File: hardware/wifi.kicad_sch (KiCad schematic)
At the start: 29 parts, among them J1 RJ45_Hanrun_HR913550A_Horizon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, U3 AP6212, Y1 26MHz

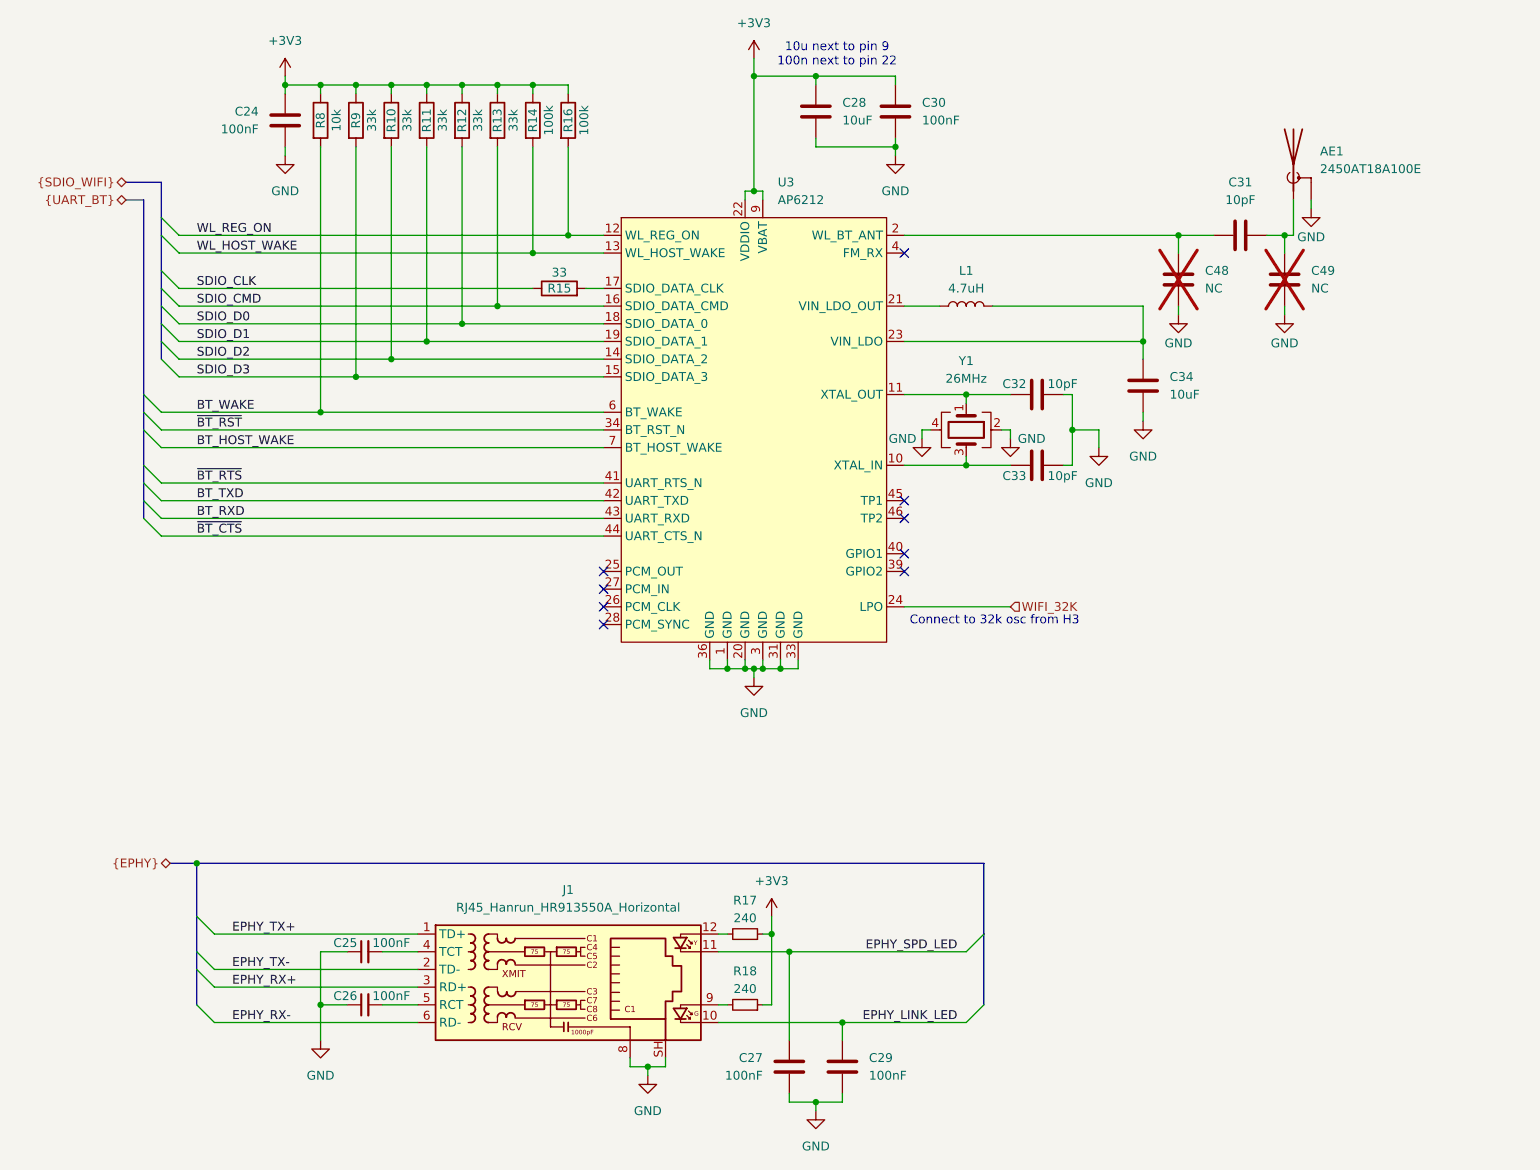
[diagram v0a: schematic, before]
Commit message: Drew most of DC DC converters
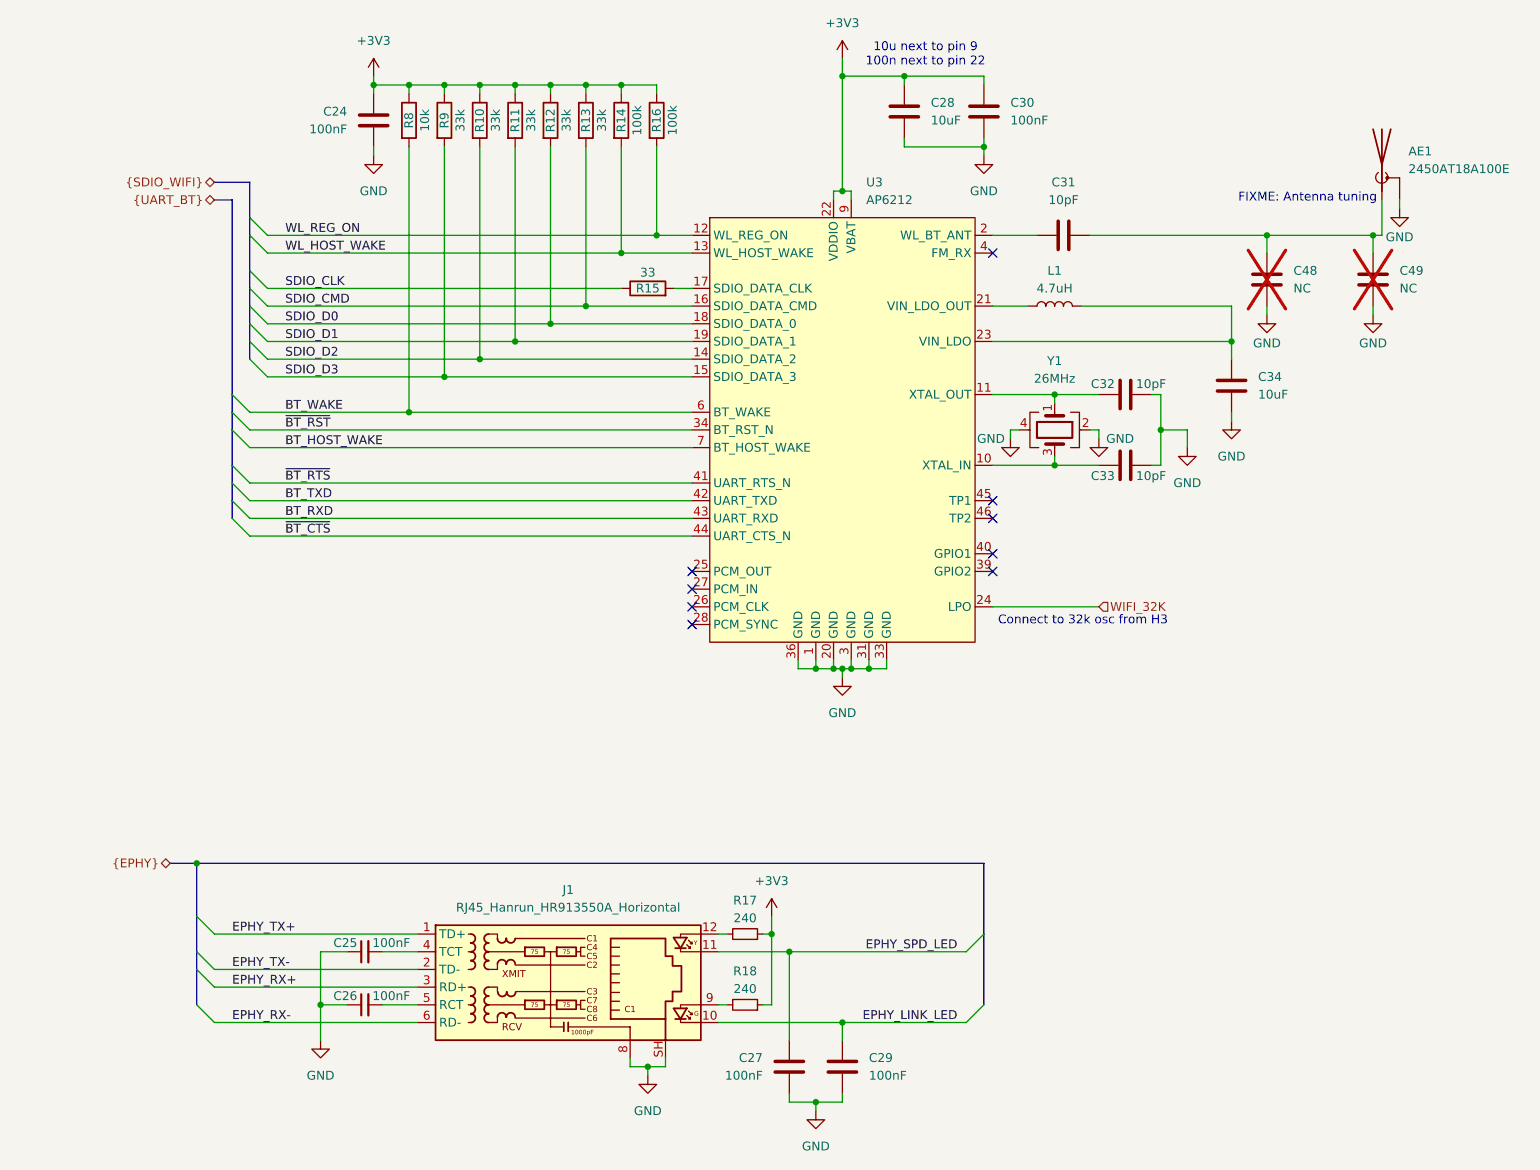
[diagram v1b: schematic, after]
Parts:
- L1: footprint cm0:L_SMD_3.0x3.0 -> (none); LCSC Part # C19734 -> (none)
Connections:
- net at AE1.1 (A), C31.2, C49.1: now also C48.1
- net at C31.1, U3.2 (WL_BT_ANT): no longer C48.1
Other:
- note added: "FIXME: Antenna tuning"
- moved on the sheet: AE1, C24, C28, C30, C31, C32, C33, C34, C48, C49, L1, R10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
